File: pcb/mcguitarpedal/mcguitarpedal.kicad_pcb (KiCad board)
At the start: 2 copper layers, 129.5 x 123 mm, 87 parts, among them J1 IN, J10 ENCODER2, J11 ENCODER3, J2 PREAMP_HEADERS, J3 BTN_MTX, J4 OUT, J5 EXP, J6 ILI9488 Module, J7 PWR_IN, J8 POT_HP_VOLUME_10k, J9 ENCODER1, SW1 SW_BYPASS, SW2 SW_TUNER, SW3 SW_PRESET, SW4 LINE_LEVEL, SW5 SW_PWR, U1 Teensy4.1, U2 Teensy Audio Board, U3 LM4562, U4 74HC148, U6 STPDWN-3P-5V, U7 STDN-3A24-ADJ, U8 74HCT595D

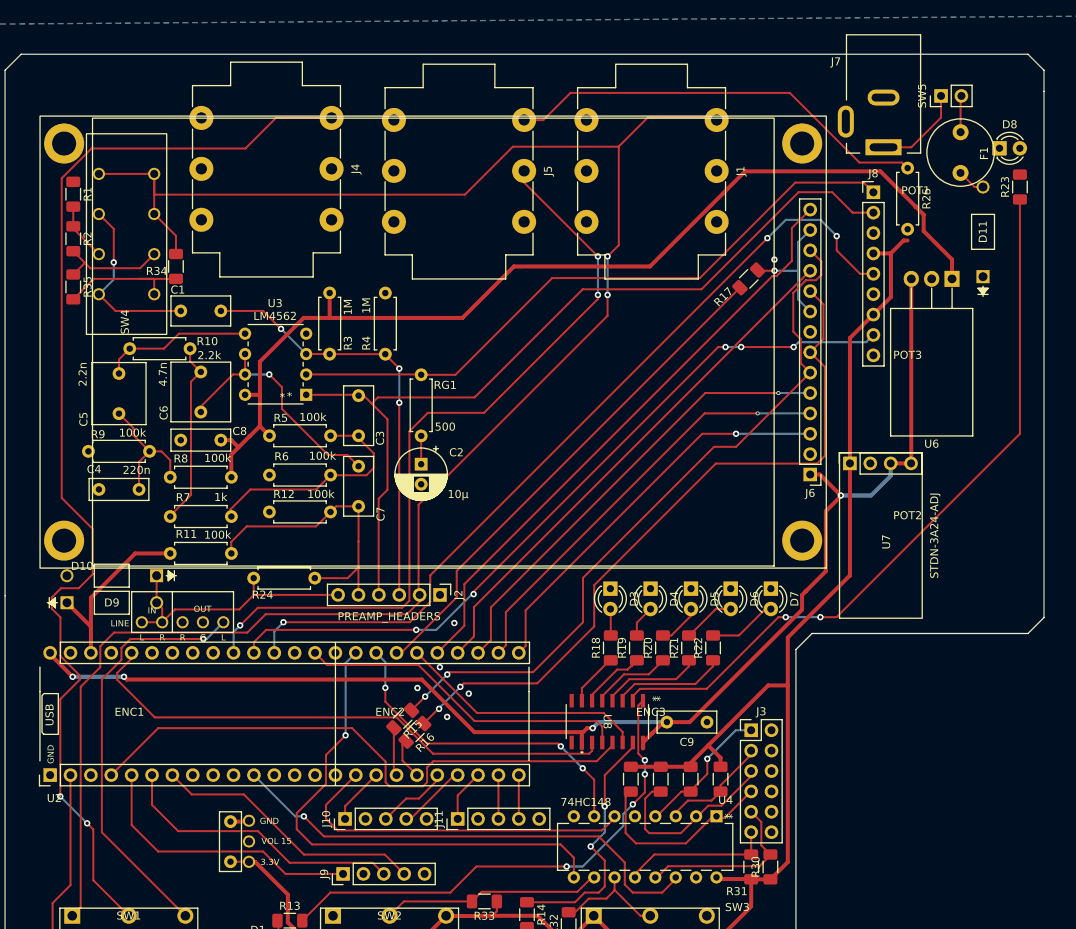
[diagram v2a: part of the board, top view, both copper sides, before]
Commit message: Reorganized power traces
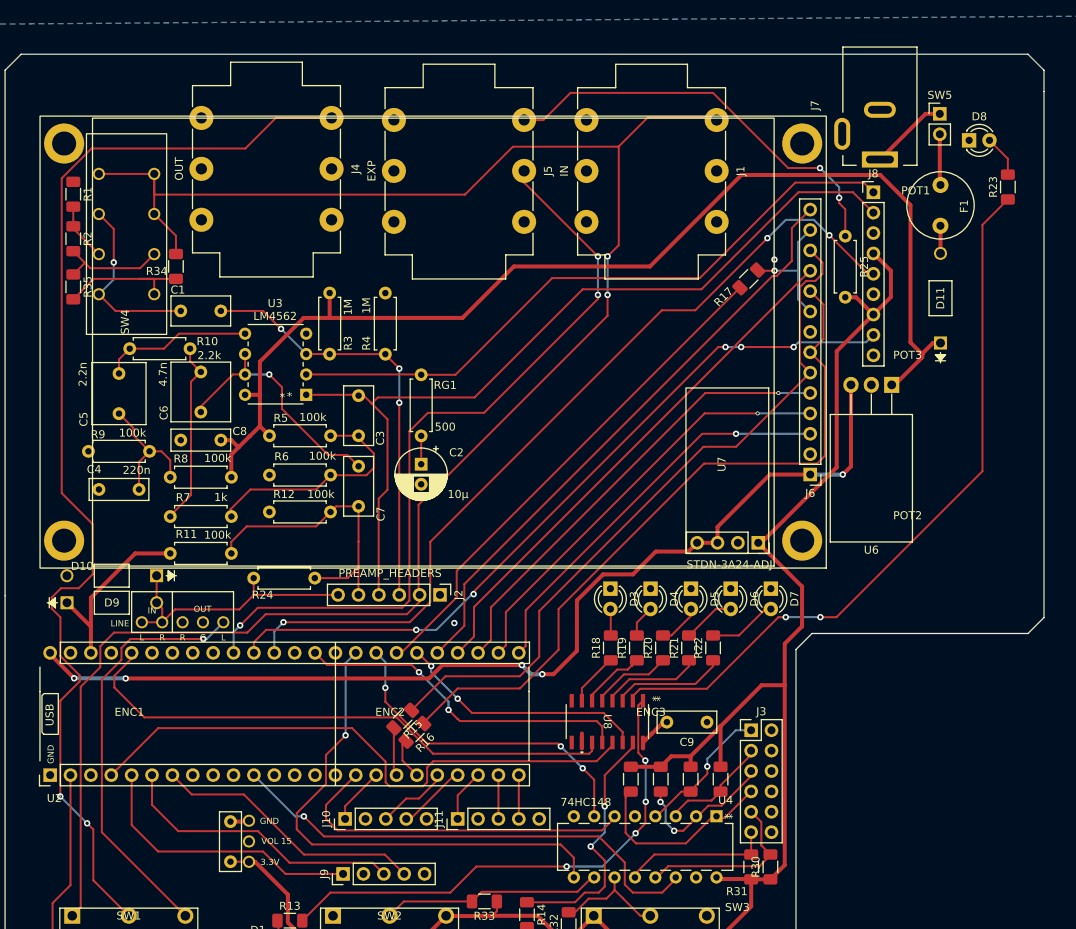
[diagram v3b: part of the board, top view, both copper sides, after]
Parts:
- moved U6 15.2 mm to (160.0, 61.2)
- moved U7 15.1 mm to (143.4, 80.9), turned to -90 degrees
- moved R25 11.5 mm to (154.2, 42.7)
- moved D11 9.83 mm to (166.1, 56.0)
- moved F1 7.04 mm to (166.1, 36.3)
- moved D8 3.92 mm to (169.7, 30.7)
- moved SW5 2.24 mm to (166.0, 27.4), turned to 0 degrees
- moved J7 1.59 mm to (158.5, 33.1)
- moved R23 1.50 mm to (174.5, 36.5)
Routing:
- net 5V: track 166.7 -> 134.8 mm, vias 4 -> 5
- net 9V: track 128.9 -> 144.6 mm
- net 3.3V: track 243.5 -> 250.6 mm
- net Net-(D8-A): track 0.00 -> 5.21 mm
- net Net-(J3-Pin_5): track 22.2 -> 18.7 mm, vias 0 -> 2
- net Net-(SW5-B): track 4.56 -> 6.36 mm
- net Net-(U8-Q1): track 62.2 -> 63.9 mm
- net Net-(SW5-A): track 11.4 -> 9.83 mm
- net /A1_VOLUME: track 104.4 -> 105.8 mm
- net Net-(J5-PadT): track 53.4 -> 52.2 mm, vias 0 -> 2
- net /LED_STR: track 68.3 -> 69.4 mm
- net /38_LED_DATA: track 31.5 -> 32.5 mm, vias 0 -> 2
- net Net-(U8-Q2): track 91.6 -> 91.0 mm
- net /SCK: track 41.6 -> 42.2 mm, vias 0 -> 2
- net Net-(J6-SDI(MOSI)): track 89.3 -> 88.7 mm, vias 2 -> 0
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
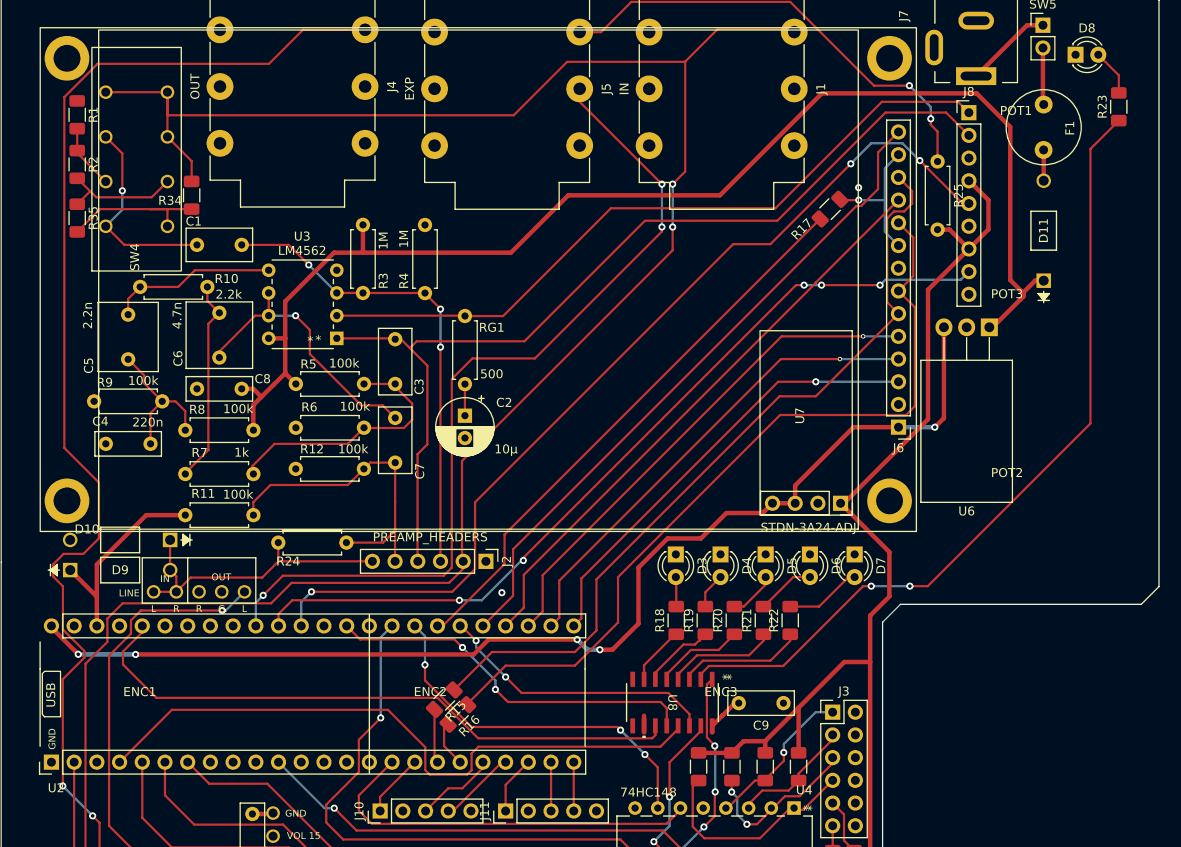
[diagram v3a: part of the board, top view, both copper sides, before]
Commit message: Routing additonal power
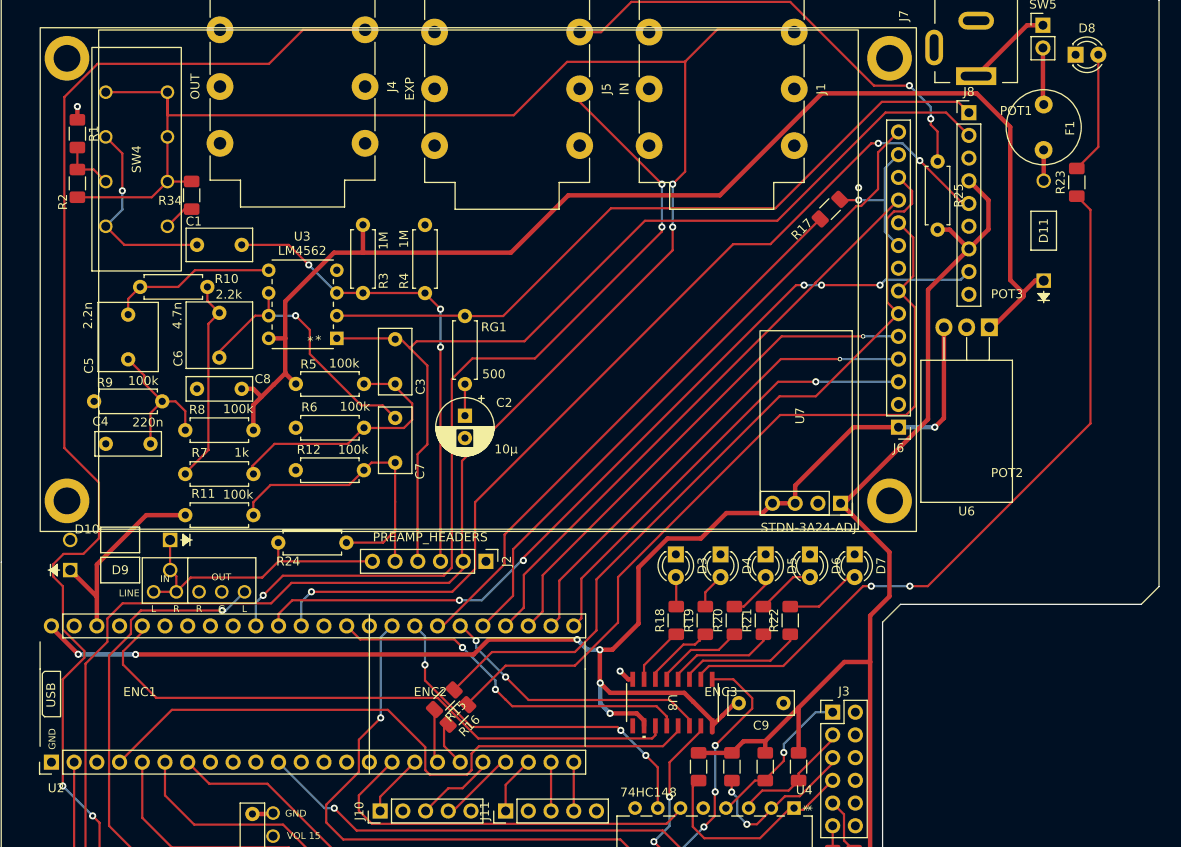
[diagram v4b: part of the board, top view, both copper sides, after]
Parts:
- removed R35: 10k, Resistor_SMD:R_1206_3216Metric_Pad1.30x1.75mm_HandSolder
- moved R23 9.67 mm to (169.8, 45.0)
- moved R2 2.12 mm to (58.0, 45.1)
- moved R1 2.11 mm to (58.0, 39.6)
- moved R12 0.15 mm to (90.1, 77.2)
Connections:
- R2 pad 2: Net-(R2-Pad2) -> /SIGNAL_IN
- SW4 pad 6: Net-(R2-Pad2) -> /SIGNAL_IN
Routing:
- net 5V: track 134.8 -> 160.4 mm, vias 5 -> 7
- net Net-(R34-Pad1): track 17.7 -> 3.50 mm
- net Net-(R2-Pad2): track 13.8 -> 0.00 mm
- net /SIGNAL_IN: track 238.4 -> 250.8 mm
- net Net-(U8-Q2): track 91.0 -> 81.8 mm
- net Net-(D8-A): track 5.21 -> 13.7 mm
- net Net-(U8-Q1): track 63.9 -> 68.1 mm
- net GND: track 2.35 -> 5.63 mm, vias 1 -> 3
- net /SCK: track 42.2 -> 41.6 mm
- net (no net): vias 1 -> 0
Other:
- board text added: "TODO: Backlight brightness PWR and status LEDs Testpoints Mounting holes Header silkscreen labels Silkscreen in general Decrease board size (Move inputs down?) Decoupling caps for U4-7 (SMD ceramic?)"
- board text removed: "TODO: PWR LEDs Testpoints Mounting holes Header silkscreen labels Decoupling caps for U4-7 (SMD ceramic?)"

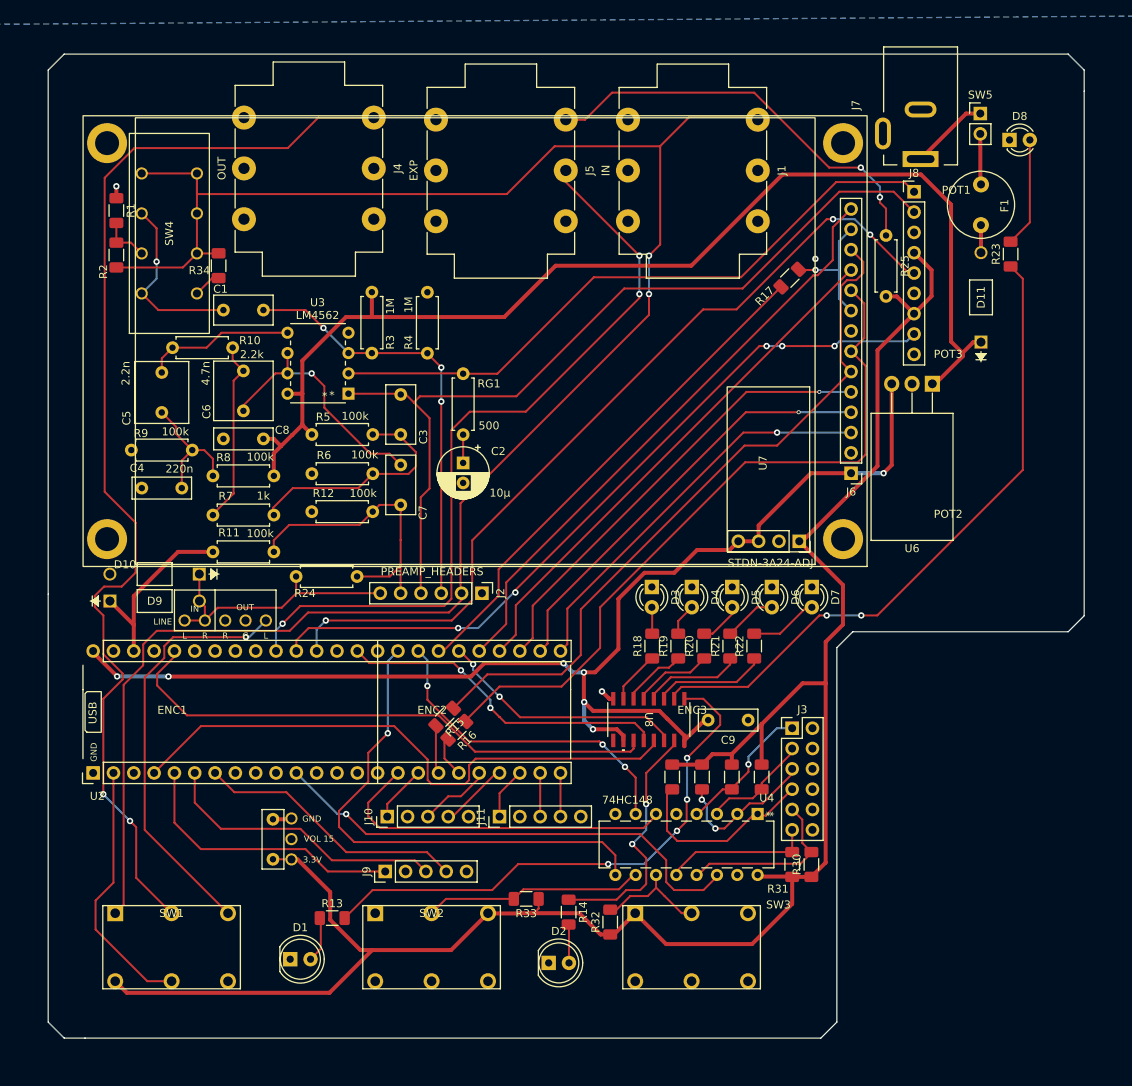
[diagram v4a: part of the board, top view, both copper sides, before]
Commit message: Backlight control, PWR leds
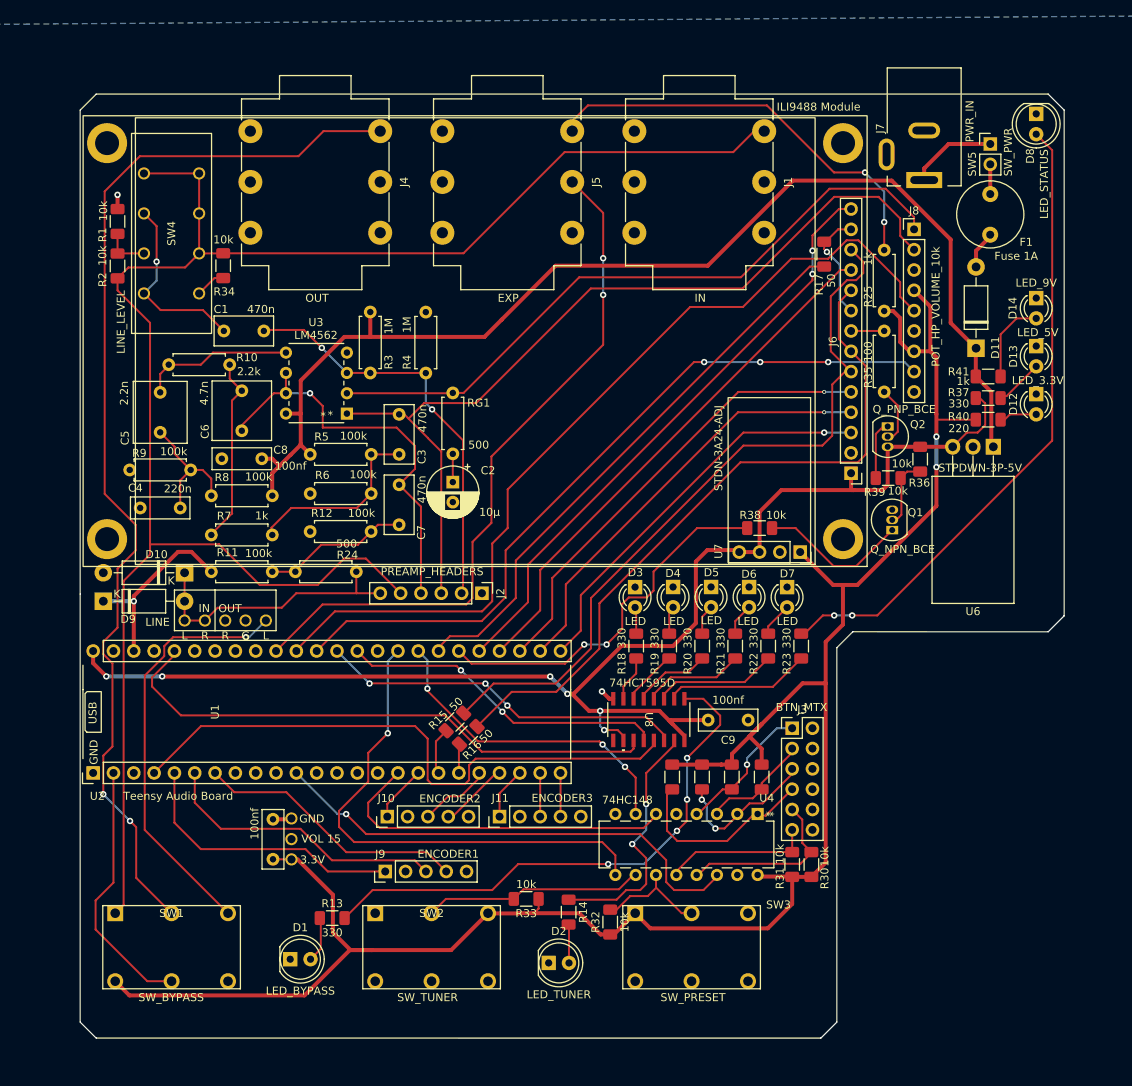
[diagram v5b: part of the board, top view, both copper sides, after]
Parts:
- added D12: LED_3.3V, mcguitarpedal:LED_D3.0mm, F.Cu at (173.0, 62.5)
- added D13: LED_5V, mcguitarpedal:LED_D3.0mm, F.Cu at (173.0, 56.5)
- added D14: LED_9V, mcguitarpedal:LED_D3.0mm, F.Cu at (173.0, 50.5)
- added Q1: Q_NPN_BCE, Package_TO_SOT_THT:TO-92_Inline, F.Cu at (155.0, 79.5)
- added Q2: Q_PNP_BCE, Package_TO_SOT_THT:TO-92_Inline, F.Cu at (154.4, 66.5)
- added R35: 100, Resistor_THT:R_Axial_DIN0207_L6.3mm_D2.5mm_P7.62mm_Horizontal, F.Cu at (154.0, 62.2)
- added R36: 10k, Resistor_SMD:R_1206_3216Metric_Pad1.30x1.75mm_HandSolder, F.Cu at (158.5, 70.6)
- added R37: 330, Resistor_SMD:R_1206_3216Metric_Pad1.30x1.75mm_HandSolder, F.Cu at (167.0, 63.0)
- added R38: 10k, Resistor_SMD:R_1206_3216Metric_Pad1.30x1.75mm_HandSolder, F.Cu at (138.4, 79.2)
- added R39: 10k, Resistor_SMD:R_1206_3216Metric_Pad1.30x1.75mm_HandSolder, F.Cu at (154.5, 73.0)
- added R40: 220, Resistor_SMD:R_1206_3216Metric_Pad1.30x1.75mm_HandSolder, F.Cu at (167.0, 65.7)
- added R41: 1k, Resistor_SMD:R_1206_3216Metric_Pad1.30x1.75mm_HandSolder, F.Cu at (167.0, 60.3)
- D10, D11, D9: footprint TI_FOOTPRINTS:DO-41_DIO -> Diode_THT:D_DO-41_SOD81_P10.16mm_Horizontal
- D8: value LED -> LED_STATUS; footprint mcguitarpedal:LED_D3.0mm -> LED_THT:LED_D5.0mm
- U1: footprint mcguitarpedal:Teensy 4.1 with audio board -> mcguitarpedal:Teensy 4.1
- U7: footprint Connector_PinSocket_2.54mm:PinSocket_1x04_P2.54mm_Vertical -> mcguitarpedal:STPDN-3A24-ADJ
- moved R23 55.6 mm to (143.6, 94.0)
- moved U6 11.0 mm to (167.6, 69.1)
- moved R24 7.74 mm to (80.4, 84.7), turned to 0 degrees
- moved R17 5.24 mm to (146.5, 45.0), turned to -90 degrees
- moved J8 4.70 mm to (157.7, 41.9)
- moved D8 4.66 mm to (173.0, 27.5), turned to -90 degrees
- moved SW5 4.01 mm to (167.3, 31.2)
- moved D7 3.09 mm to (141.9, 86.6)
- moved D6 2.84 mm to (137.1, 86.6)
- moved RG1 2.73 mm to (100.1, 62.4)
- moved C2 2.73 mm to (100.1, 73.5)
- moved J7 2.66 mm to (159.0, 35.8)
- moved D5 2.64 mm to (132.4, 86.6)
- moved C1 2.61 mm to (76.5, 54.6)
- moved C4 2.49 mm to (66.0, 76.7)
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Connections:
- net /24_BTN_MTX_GS renamed /9_BTN_MTX_GS
- J2 pad 2: /SIGNAL_IN -> /preamp/STAGE1_IN
- J2 pad 3: /preamp/STAGE1_IN -> /preamp/STAGE1_OUT
- J2 pad 4: /preamp/STAGE1_OUT -> /preamp/STAGE2_OUT
- J2 pad 5: /preamp/PREAMP_OUT -> /SIGNAL_IN
- J8 pad 5: /A1_VOLUME -> /A2_VOLUME
- J8 pad 8: /A2_POT -> /A1_POT
- U1 pad 30: /38_LED_DATA -> /38_BACKLIGHT_PWM
- U1 pad 36: /14_BACKLIGHT_PWM -> /14_LED_DATA
- U1 pad 37: /A1_VOLUME -> /A1_POT
- U1 pad 38: /A2_POT -> /A2_VOLUME
- U8 pad 14: /38_LED_DATA -> /14_LED_DATA
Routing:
- net /A2_VOLUME: track 0.00 -> 110.2 mm
- net /A1_VOLUME: track 105.8 -> 0.00 mm, vias 3 -> 0
- net /A2_POT: track 94.6 -> 0.00 mm, vias 5 -> 0
- net /A1_POT: track 0.00 -> 93.6 mm, vias 0 -> 3
- net Net-(D8-A): track 13.7 -> 80.1 mm, vias 0 -> 2
- net Net-(U8-Q2): track 81.8 -> 17.7 mm, vias 2 -> 0
- net /38_BACKLIGHT_PWM: track 0.00 -> 46.9 mm, vias 0 -> 2
- net /14_LED_DATA: track 0.00 -> 45.2 mm, vias 0 -> 3
- net /38_LED_DATA: track 32.1 -> 0.00 mm, vias 2 -> 0
- net /SIGNAL_IN: track 250.8 -> 224.1 mm, vias 2 -> 0
- net /preamp/STAGE2_OUT: track 30.9 -> 51.2 mm
- net Net-(Q1-B): track 0.00 -> 18.9 mm
- net /preamp/PREAMP_OUT: track 35.9 -> 18.3 mm
- net 5V: track 160.4 -> 172.3 mm, vias 7 -> 6
- net Net-(D14-A): track 0.00 -> 10.5 mm
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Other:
- board size 129.5 x 123 mm -> 123 x 118 mm
